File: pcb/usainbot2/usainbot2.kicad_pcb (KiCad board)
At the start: 2 copper layers, 147.3 x 132.1 mm, 13 parts, among them J1 BT_MOD, J2 QTR1-L, J3 QTR1-R, J4 QTR8, J5 SWITCH, M1 Conn_01x02_Male, M2 Conn_01x02_Male, SW1 BTN1, SW2 BTN2, U1 TB6612FNG_breakout

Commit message: update pcb, falta rutear
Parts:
- removed J5: SWITCH, Connector_PinHeader_2.54mm:PinHeader_1x03_P2.54mm_Vertical
- added C1: C, Capacitor_SMD:C_0805_2012Metric_Pad1.18x1.45mm_HandSolder, B.Cu at (74.3, 121.0)
- added C2: C, Capacitor_SMD:C_0805_2012Metric_Pad1.18x1.45mm_HandSolder, B.Cu at (68.7, 121.0)
- added D1: WS2812B, LED_SMD:LED_WS2812B_PLCC4_5.0x5.0mm_P3.2mm, F.Cu at (81.7, 92.2)
- added U2: LM7805_TO220, Package_TO_SOT_THT:TO-220-3_Vertical, F.Cu at (73.8, 116.2)
- BATTJ6: footprint Connector_PinHeader_2.54mm:PinHeader_1x02_P2.54mm_Horizontal -> Connector_Molex:Molex_KK-254_AE-6410-02A_1x02_P2.54mm_Vertical
- J2, J3: footprint Connector_PinHeader_2.54mm:PinHeader_1x03_P2.54mm_Vertical -> Connector_PinHeader_2.54mm:PinHeader_1x03_P2.54mm_Horizontal
- J4: value QTR8 -> QTR-6A; footprint Connector_PinSocket_2.54mm:PinSocket_1x11_P2.54mm_Horizontal -> Connector_PinHeader_2.54mm:PinHeader_1x09_P2.54mm_Horizontal
- M1, M2: footprint Connector_PinHeader_2.54mm:PinHeader_1x02_P2.54mm_Horizontal -> Connector_PinHeader_2.54mm:PinHeader_1x02_P2.54mm_Vertical
- R0: moved to B.Cu
- SW1: value BTN1 -> SW_SPDT; footprint Button_Switch_THT:SW_PUSH_6mm -> usainbot:TOGGLE_RA
- moved J4 98.7 mm to (85.1, 45.0), turned to 90 degrees
- moved SW2 98.6 mm to (117.6, 87.4), turned to -90 degrees
- moved J2 86.2 mm to (26.9, 103.8), turned to 180 degrees
- moved M2 86.1 mm to (120.8, 148.2)
- moved U1 79.7 mm to (98.4, 153.2)
- moved SW1 72.9 mm to (75.6, 169.2)
- moved J3 68.5 mm to (169.9, 98.6)
- moved M1 67.6 mm to (82.6, 147.5), turned to 180 degrees
- moved R0 54.3 mm to (98.6, 140.3), turned to 180 degrees
- moved ArduinoNano1 49.4 mm to (106.2, 103.1), turned to 180 degrees
- moved BATTJ6 43.6 mm to (119.5, 159.9), turned to 0 degrees
- moved J1 28.4 mm to (114.9, 100.7), turned to 90 degrees
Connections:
- ArduinoNano1 pad 10: /BTN1 -> /BTN2
- ArduinoNano1 pad 11: /BTN2 -> unconnected-(ArduinoNano1-Pad11)
- ArduinoNano1 pad 12: unconnected-(ArduinoNano1-Pad12) -> Net-(ArduinoNano1-Pad12)
- ArduinoNano1 pad 25: Net-(ArduinoNano1-Pad25) -> /A6
- ArduinoNano1 pad 26: Net-(ArduinoNano1-Pad26) -> /A7
- ArduinoNano1 pad 27: +5V -> Net-(D1-Pad1)
- ArduinoNano1 pad 5: Net-(ArduinoNano1-Pad5) -> unconnected-(ArduinoNano1-Pad5)
- ArduinoNano1 pad 6: Net-(ArduinoNano1-Pad6) -> unconnected-(ArduinoNano1-Pad6)
- J2 pad 3: Net-(ArduinoNano1-Pad5) -> /A7
- J3 pad 3: Net-(ArduinoNano1-Pad6) -> /A6
- J4 pad 7: Net-(ArduinoNano1-Pad25) -> unconnected-(J4-Pad7)
- J4 pad 8: Net-(ArduinoNano1-Pad26) -> +5V
- J4 pad 9: unconnected-(J4-Pad9) -> GND
- SW1 pad 2: /BTN1 -> VCC
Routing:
- net +5V: track 0.00 -> 276.5 mm
- net VCC: track 0.00 -> 69.3 mm
- net /A7: track 0.00 -> 66.4 mm
- net Net-(ArduinoNano1-Pad24): track 0.00 -> 60.9 mm
- net Net-(BATTJ6-Pad1): track 0.00 -> 60.2 mm
- net Net-(ArduinoNano1-Pad23): track 0.00 -> 58.8 mm
- net Net-(ArduinoNano1-Pad22): track 0.00 -> 57.8 mm
- net Net-(ArduinoNano1-Pad12): track 0.00 -> 52.1 mm, vias 0 -> 1
- net Net-(ArduinoNano1-Pad21): track 0.00 -> 41.3 mm
- net Net-(ArduinoNano1-Pad20): track 0.00 -> 38.1 mm
- net Net-(ArduinoNano1-Pad19): track 0.00 -> 33.7 mm
- net Net-(D1-Pad1): track 0.00 -> 14.4 mm, vias 0 -> 1
- net Net-(M1-Pad1): track 0.00 -> 13.3 mm
- net Net-(M1-Pad2): track 0.00 -> 13.2 mm
- net GND: track 0.00 -> 8.44 mm
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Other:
- board size 147.3 x 132.1 mm -> 157 x 150 mm
- rule pad_to_mask_clearance: 0 -> 0.0508

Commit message: last pcb update
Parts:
- J2, J3: moved to B.Cu
- SW1: footprint usainbot:TOGGLE_RA -> usainbot:SPST slide switch
- SW2: value BTN2 -> SW_Push; footprint Button_Switch_THT:SW_PUSH_6mm -> Button_Switch_SMD:SW_Push_1P1T_NO_Vertical_Wuerth_434133025816
- moved BATTJ6 48.1 mm to (71.8, 154.3)
- moved J1 43.1 mm to (114.9, 143.8)
- moved SW2 36.6 mm to (81.3, 82.5), turned to 90 degrees
- moved R0 33.9 mm to (65.4, 133.3), turned to 90 degrees
- moved M2 25.0 mm to (106.7, 168.9), turned to -90 degrees
- moved C1 12.2 mm to (62.2, 122.4), turned to 90 degrees
- moved U2 8.88 mm to (67.0, 121.9), turned to 90 degrees
- moved M1 8.85 mm to (83.8, 156.2)
- moved C2 7.77 mm to (62.2, 116.8), turned to -90 degrees
- moved J2 7.31 mm to (32.0, 98.6)
- moved J3 7.13 mm to (164.8, 103.6)
- moved SW1 5.37 mm to (76.2, 163.8), turned to 180 degrees
- moved U1 1.78 mm to (98.4, 154.9)
- turned D1 to 180 degrees
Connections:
- ArduinoNano1 pad 10: /BTN2 -> unconnected-(ArduinoNano1-Pad10)
- ArduinoNano1 pad 13: Net-(ArduinoNano1-Pad13) -> Net-(U1-Pad15)
- ArduinoNano1 pad 15: Net-(ArduinoNano1-Pad15) -> Net-(U1-Pad11)
- ArduinoNano1 pad 5: unconnected-(ArduinoNano1-Pad5) -> Net-(ArduinoNano1-Pad5)
- ArduinoNano1 pad 6: unconnected-(ArduinoNano1-Pad6) -> Net-(ArduinoNano1-Pad6)
- ArduinoNano1 pad 8: Net-(ArduinoNano1-Pad8) -> Net-(U1-Pad10)
- ArduinoNano1 pad 9: Net-(ArduinoNano1-Pad9) -> Net-(U1-Pad16)
- J2 pad 2: +5V -> Net-(ArduinoNano1-Pad5)
- J2 pad 3: /A7 -> +5V
- J3 pad 2: +5V -> Net-(ArduinoNano1-Pad6)
- J3 pad 3: /A6 -> +5V
- SW1 pad 2: VCC -> Net-(BATTJ6-Pad1)
- SW1 pad 3: Net-(BATTJ6-Pad1) -> VCC
- SW2 pad 1: unconnected-(SW2-Pad1) -> /A7
- SW2 pad 2: /BTN2 -> GND
- U1 pad 10: Net-(ArduinoNano1-Pad9) -> Net-(U1-Pad10)
- U1 pad 11: Net-(ArduinoNano1-Pad13) -> Net-(U1-Pad11)
- U1 pad 15: Net-(ArduinoNano1-Pad15) -> Net-(U1-Pad15)
- U1 pad 16: Net-(ArduinoNano1-Pad8) -> Net-(U1-Pad16)
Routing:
- net Net-(U1-Pad11): track 0.00 -> 128.9 mm
- net Net-(ArduinoNano1-Pad6): track 0.00 -> 123.9 mm, vias 0 -> 1
- net GND: track 8.44 -> 128.0 mm
- net Net-(ArduinoNano1-Pad14): track 2.91 -> 122.2 mm
- net Net-(U1-Pad15): track 0.00 -> 107.9 mm
- net Net-(ArduinoNano1-Pad5): track 0.00 -> 99.3 mm, vias 0 -> 1
- net Net-(U1-Pad10): track 0.00 -> 97.6 mm, vias 0 -> 2
- net Net-(ArduinoNano1-Pad16): track 3.52 -> 98.3 mm
- net Net-(ArduinoNano1-Pad7): track 3.12 -> 80.9 mm, vias 0 -> 2
- net Net-(U1-Pad16): track 0.00 -> 73.0 mm
- net VCC: track 69.3 -> 131.3 mm, vias 0 -> 2
- net Net-(ArduinoNano1-Pad2): track 0.00 -> 49.8 mm
- net /A7: track 66.4 -> 17.1 mm
- net Net-(BATTJ6-Pad1): track 60.2 -> 11.3 mm
- net Net-(ArduinoNano1-Pad1): track 0.00 -> 46.4 mm
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- added copper zone on B.Cu, net GND
- added copper zone on F.Cu, net GND
- added copper zone on B.Cu, net GNDPWR
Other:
- board size 157 x 150 mm -> 157 x 152.5 mm

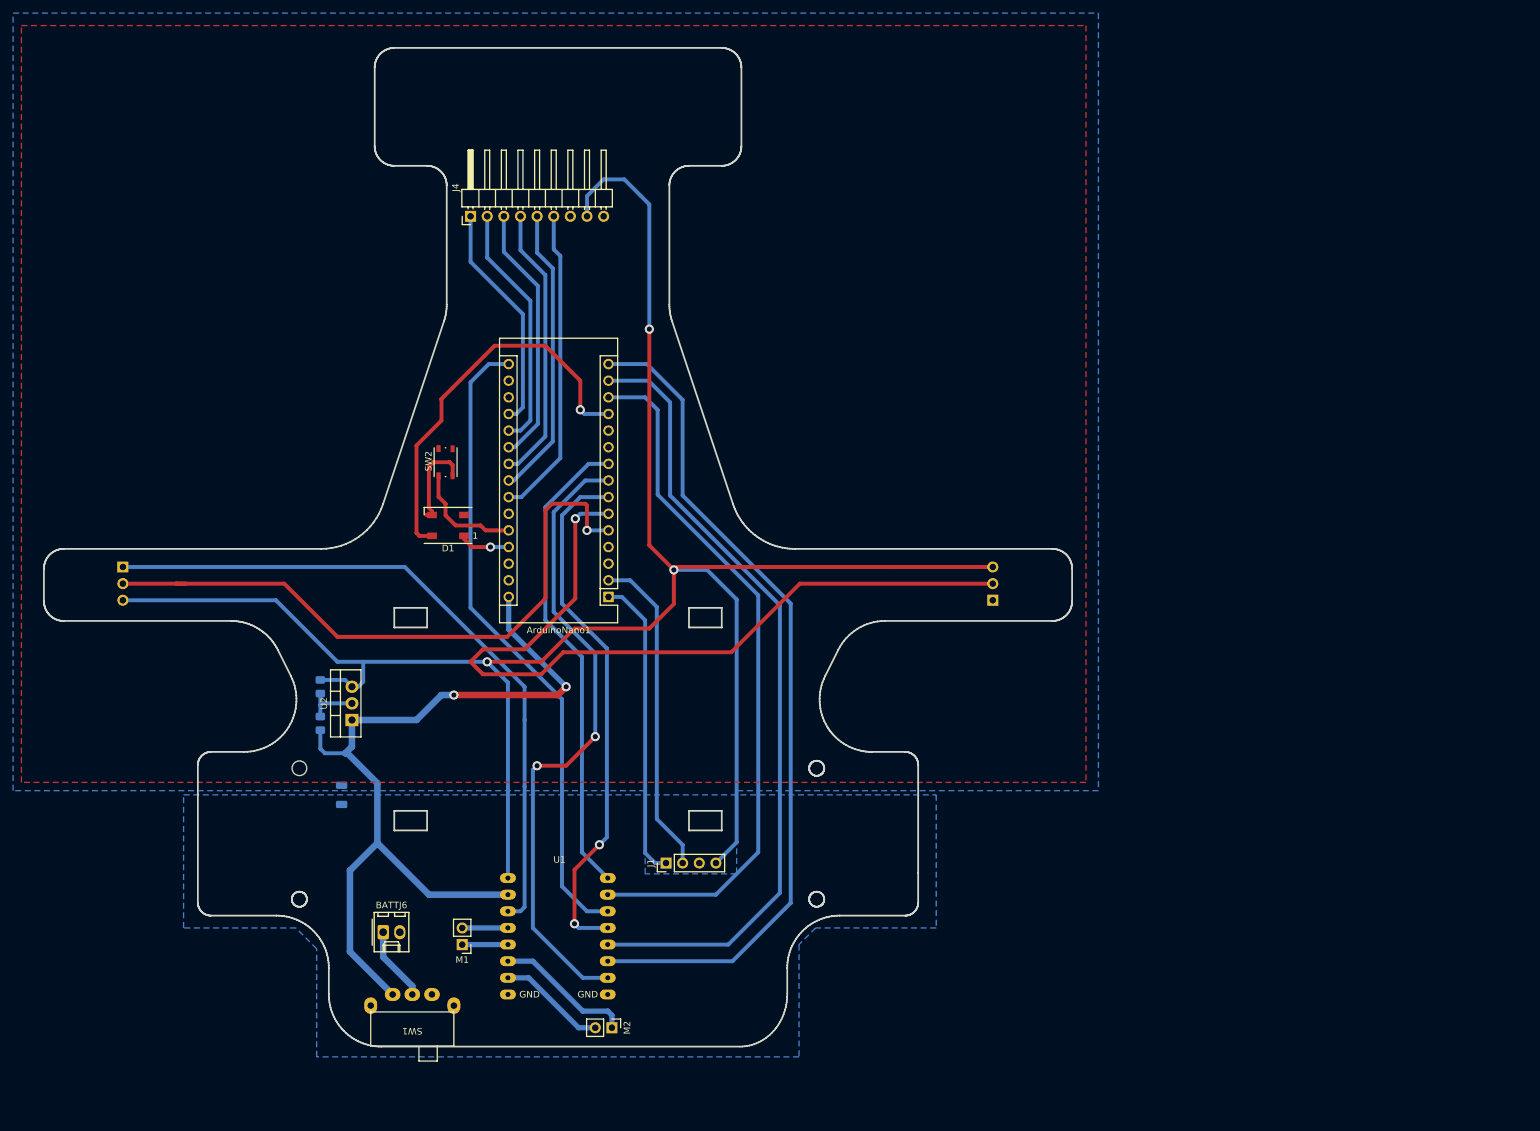
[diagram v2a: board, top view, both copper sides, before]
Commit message: robot racer v2.1 kicad
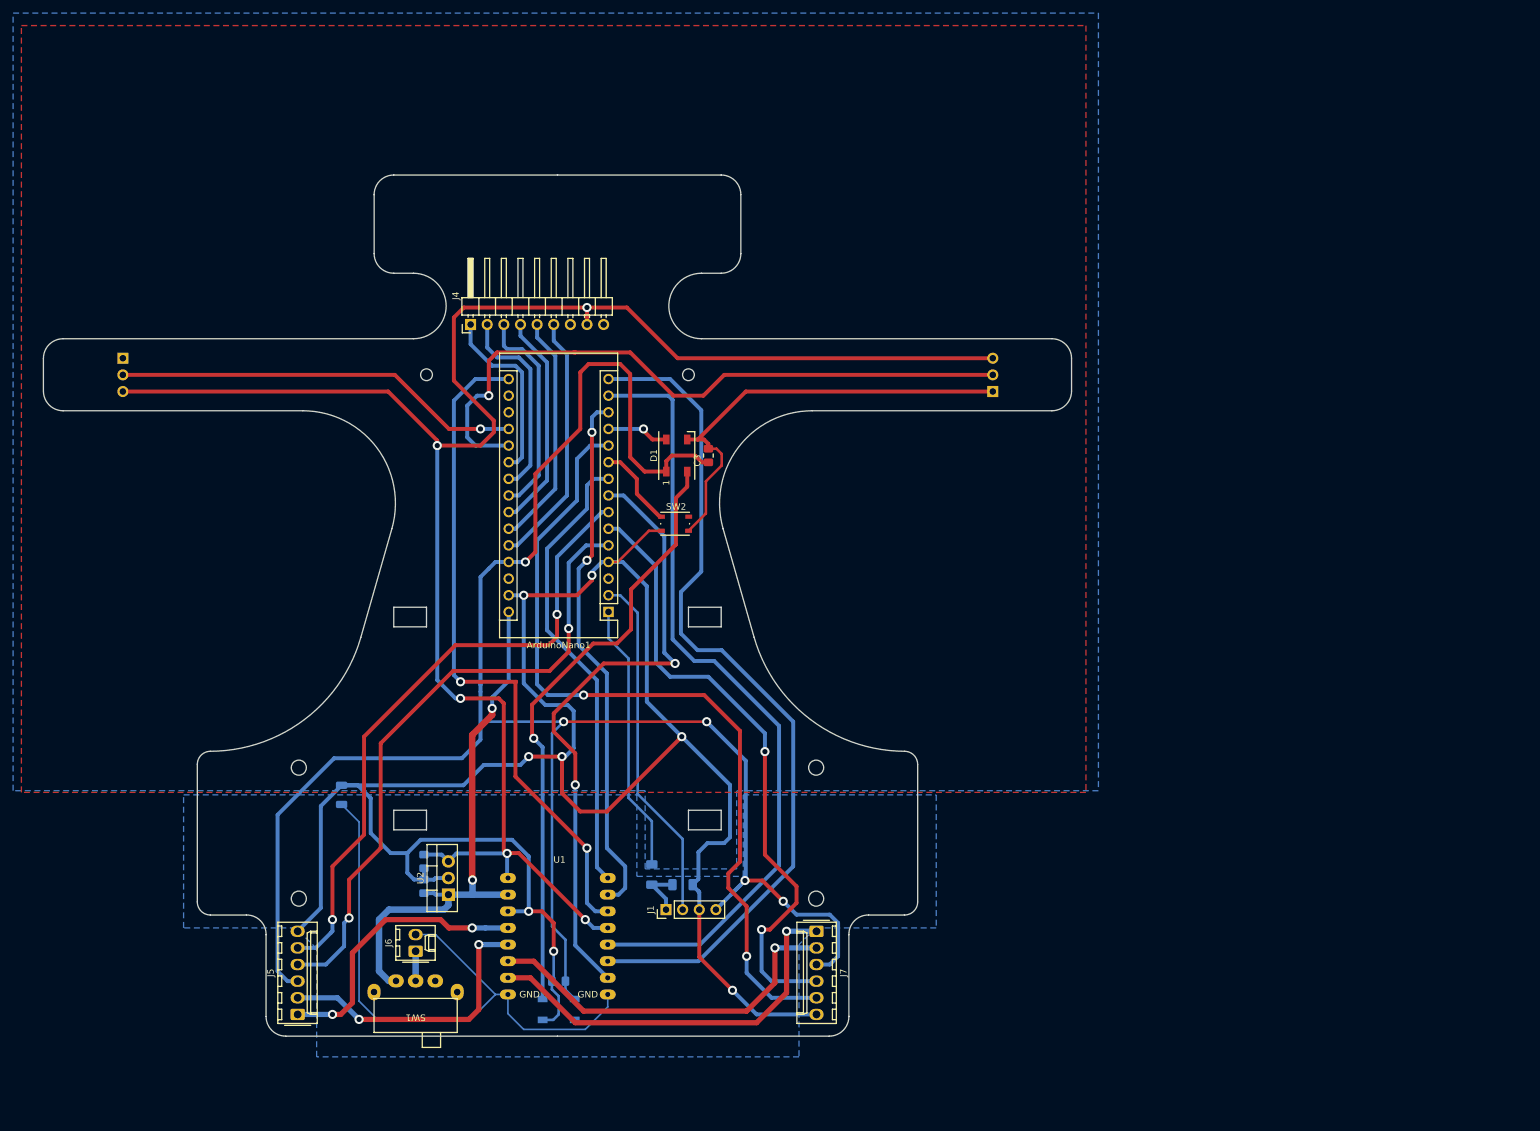
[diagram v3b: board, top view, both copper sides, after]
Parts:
- removed BATTJ6: BATT, Connector_Molex:Molex_KK-254_AE-6410-02A_1x02_P2.54mm_Vertical
- removed M1, M2: Conn_01x02_Male, Connector_PinHeader_2.54mm:PinHeader_1x02_P2.54mm_Vertical
- added C3: 0.1u, Capacitor_SMD:C_0805_2012Metric_Pad1.18x1.45mm_HandSolder, F.Cu at (121.4, 81.5)
- added C4: 0.1u, Capacitor_SMD:C_0805_2012Metric_Pad1.18x1.45mm_HandSolder, B.Cu at (98.6, 161.8)
- added D2: WS2812B, LED_SMD:LED_WS2812B_PLCC4_5.0x5.0mm_P3.2mm, B.Cu at (98.6, 166.1)
- added J5: M1, Connector_Molex:Molex_KK-254_AE-6410-06A_1x06_P2.54mm_Vertical, F.Cu at (58.7, 166.9)
- added J6: BATT, Connector_Molex:Molex_KK-254_AE-6410-02A_1x02_P2.54mm_Vertical, F.Cu at (76.7, 157.2)
- added J7: M2, Connector_Molex:Molex_KK-254_AE-6410-06A_1x06_P2.54mm_Vertical, F.Cu at (137.9, 154.2)
- added R1: 1K, Resistor_SMD:R_1206_3216Metric_Pad1.30x1.75mm_HandSolder, B.Cu at (112.8, 145.5)
- added R2: 2K, Resistor_SMD:R_1206_3216Metric_Pad1.30x1.75mm_HandSolder, B.Cu at (117.5, 147.1)
- C1: value C -> 0.22u
- C2: value C -> 0.1u
- moved D1 36.5 mm to (116.6, 81.5), turned to 90 degrees
- moved SW2 36.3 mm to (116.3, 91.9), turned to 0 degrees
- moved J2 31.9 mm to (32.0, 66.7)
- moved J3 31.9 mm to (164.8, 71.8)
- moved C2 31.0 mm to (78.0, 143.5)
- moved U2 30.5 mm to (81.7, 148.6)
- moved C1 29.5 mm to (78.0, 147.3)
- moved J4 16.5 mm to (85.1, 61.5)
- moved J1 7.11 mm to (114.9, 150.9)
- moved ArduinoNano1 2.29 mm to (106.2, 105.4)
- moved SW1 2.13 mm to (76.7, 161.8)
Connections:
- ArduinoNano1 pad 10: unconnected-(ArduinoNano1-Pad10) -> /D7
- ArduinoNano1 pad 11: unconnected-(ArduinoNano1-Pad11) -> /D8
- ArduinoNano1 pad 19: Net-(ArduinoNano1-Pad19) -> /QTR-L
- ArduinoNano1 pad 20: Net-(ArduinoNano1-Pad20) -> /QTR-R
- ArduinoNano1 pad 25: /A6 -> Net-(ArduinoNano1-Pad25)
- ArduinoNano1 pad 26: /A7 -> Net-(ArduinoNano1-Pad26)
- ArduinoNano1 pad 27: Net-(ArduinoNano1-Pad27) -> +5VD
- ArduinoNano1 pad 5: Net-(ArduinoNano1-Pad5) -> /D2
- ArduinoNano1 pad 6: Net-(ArduinoNano1-Pad6) -> /D3
- ArduinoNano1 pad 7: Net-(ArduinoNano1-Pad7) -> /D4
- D1 pad 1: Net-(ArduinoNano1-Pad27) -> +5VD
- D1 pad 2: unconnected-(D1-Pad2) -> Net-(D1-Pad2)
- J1 pad 1: Net-(ArduinoNano1-Pad1) -> Net-(J1-Pad1)
- J1 pad 4: +5V -> +5VD
- J2 pad 2: Net-(ArduinoNano1-Pad5) -> /QTR-L
- J3 pad 2: Net-(ArduinoNano1-Pad6) -> /QTR-R
- J4 pad 1: Net-(ArduinoNano1-Pad19) -> Net-(ArduinoNano1-Pad21)
- J4 pad 2: Net-(ArduinoNano1-Pad20) -> Net-(ArduinoNano1-Pad22)
- J4 pad 3: Net-(ArduinoNano1-Pad21) -> Net-(ArduinoNano1-Pad23)
- J4 pad 4: Net-(ArduinoNano1-Pad22) -> Net-(ArduinoNano1-Pad24)
- J4 pad 5: Net-(ArduinoNano1-Pad23) -> Net-(ArduinoNano1-Pad25)
- J4 pad 6: Net-(ArduinoNano1-Pad24) -> Net-(ArduinoNano1-Pad26)
- SW2 pad 1: /A7 -> /D7
- U1 pad 13: Net-(ArduinoNano1-Pad7) -> +5V
- U1 pad 4: Net-(M1-Pad2) -> /ML-1
- U1 pad 5: Net-(M1-Pad1) -> /ML-2
- U1 pad 6: Net-(M2-Pad1) -> /MR-2
- U1 pad 7: Net-(M2-Pad2) -> /MR-1
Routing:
- net +5VD: track 0.00 -> 312.2 mm, vias 0 -> 5
- net GND: track 128.0 -> 395.8 mm, vias 0 -> 8
- net /D8: track 0.00 -> 127.6 mm, vias 0 -> 2
- net Net-(ArduinoNano1-Pad6): track 123.9 -> 0.00 mm, vias 1 -> 0
- net /QTR-R: track 0.00 -> 102.8 mm, vias 0 -> 1
- net Net-(ArduinoNano1-Pad5): track 99.3 -> 0.00 mm, vias 1 -> 0
- net /D4: track 0.00 -> 96.9 mm, vias 0 -> 2
- net /D2: track 0.00 -> 96.8 mm, vias 0 -> 2
- net /D3: track 0.00 -> 95.7 mm, vias 0 -> 2
- net GNDPWR: track 0.00 -> 95.3 mm
- net Net-(D1-Pad2): track 0.00 -> 93.1 mm, vias 0 -> 1
- net Net-(ArduinoNano1-Pad7): track 80.9 -> 0.00 mm, vias 2 -> 0
- net /QTR-L: track 0.00 -> 62.3 mm, vias 0 -> 1
- net /MR-1: track 0.00 -> 61.2 mm, vias 0 -> 1
- net /MR-2: track 0.00 -> 57.4 mm, vias 0 -> 1
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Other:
- board size 157 x 152.5 mm -> 157 x 131.5 mm
- rule pad_to_mask_clearance: 0.0508 -> 0

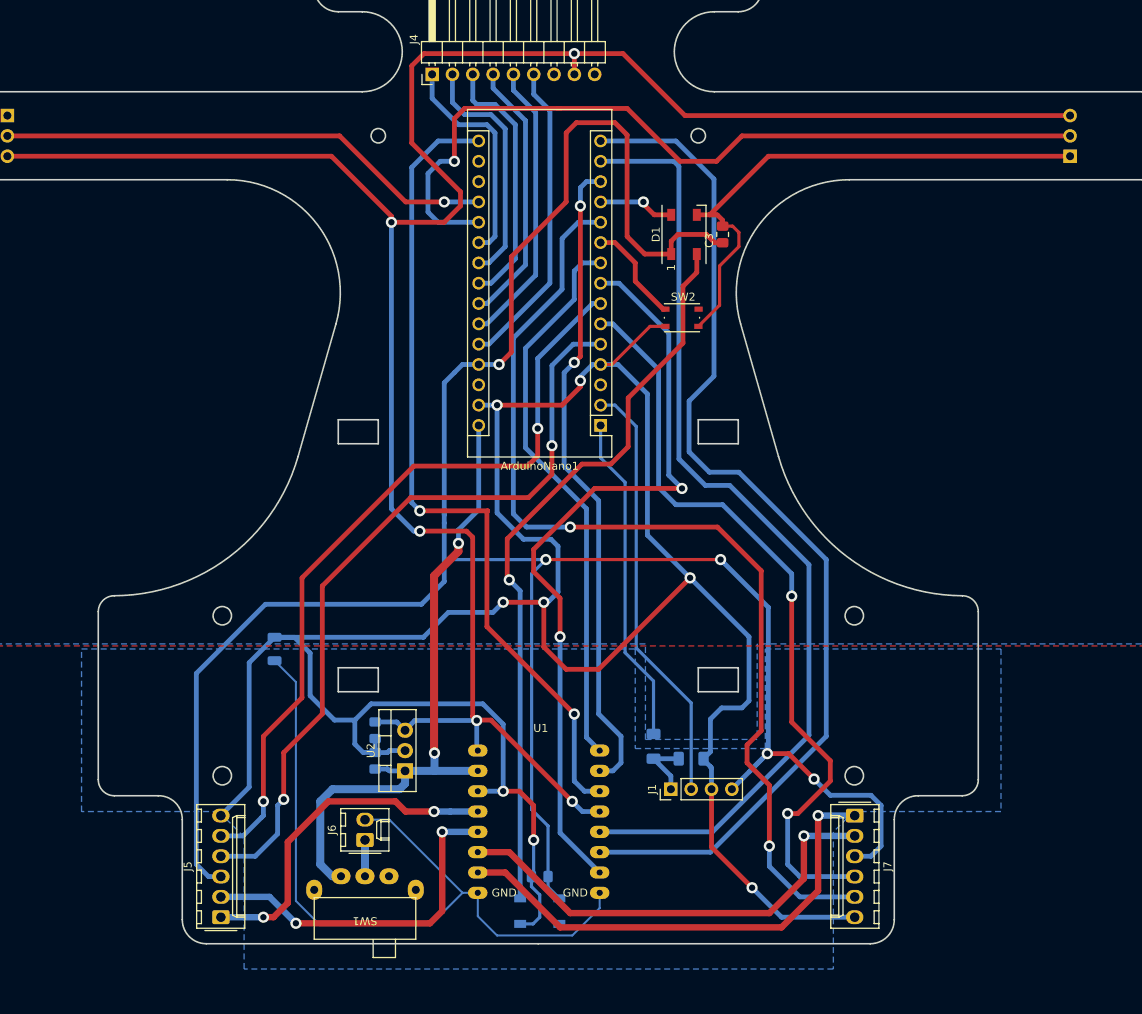
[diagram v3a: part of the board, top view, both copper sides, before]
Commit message: add led and add top pwrgnd isolation copper
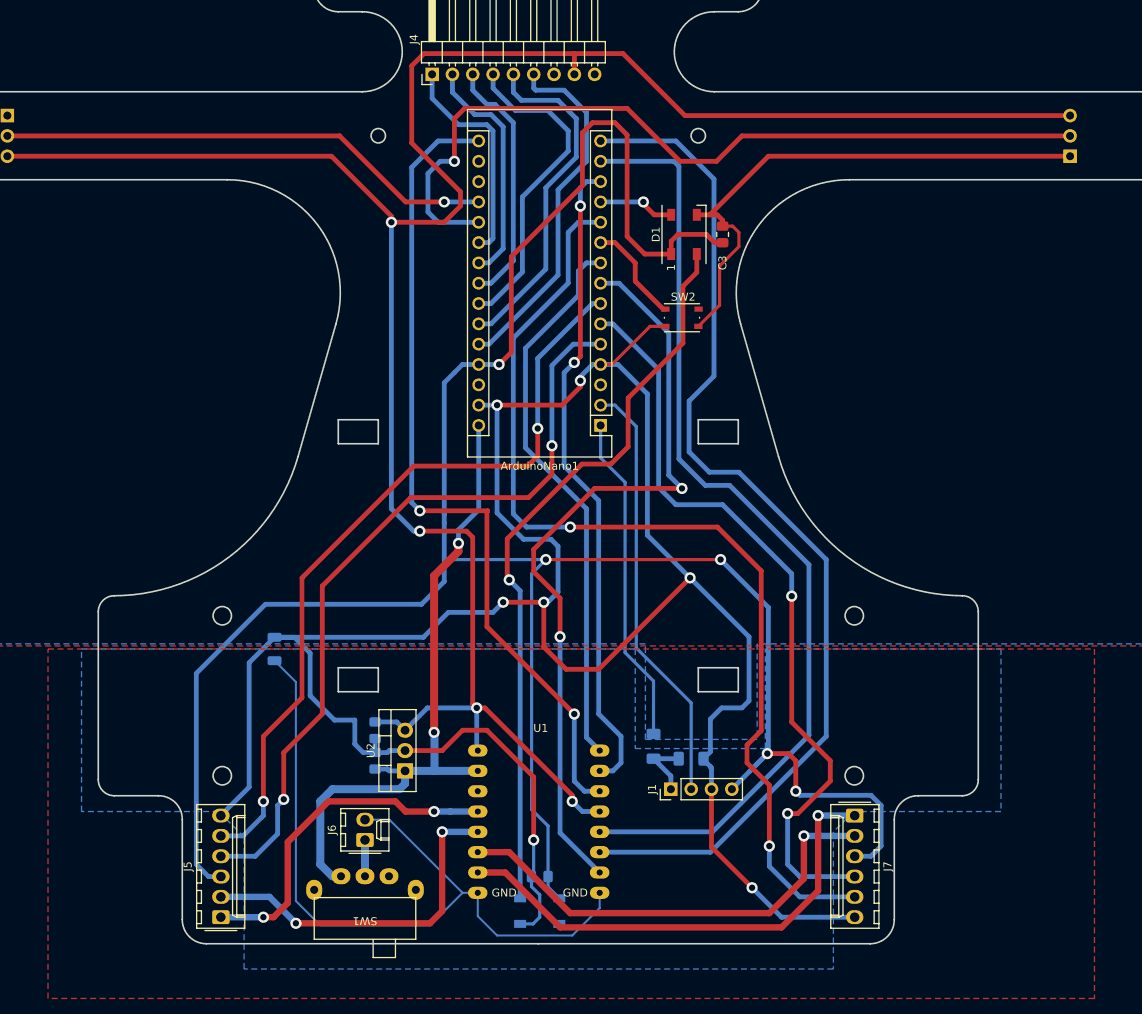
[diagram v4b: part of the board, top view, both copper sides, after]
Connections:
- U1 pad 3: GND -> GNDPWR
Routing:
- net GND: track 395.8 -> 382.4 mm, vias 8 -> 7
- net Net-(ArduinoNano1-Pad25): track 35.9 -> 43.1 mm
- net Net-(ArduinoNano1-Pad24): track 33.3 -> 40.4 mm
- net Net-(ArduinoNano1-Pad26): track 39.0 -> 44.9 mm
- net +5V: track 278.3 -> 280.0 mm, vias 5 -> 4
- net +5VD: track 312.2 -> 313.2 mm
- net Net-(ArduinoNano1-Pad23): track 32.4 -> 31.5 mm
- net Net-(ArduinoNano1-Pad22): track 30.4 -> 29.4 mm
- added copper zone on F.Cu, net GNDPWR
